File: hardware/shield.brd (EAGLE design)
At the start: 100 x 80 mm, 21 parts

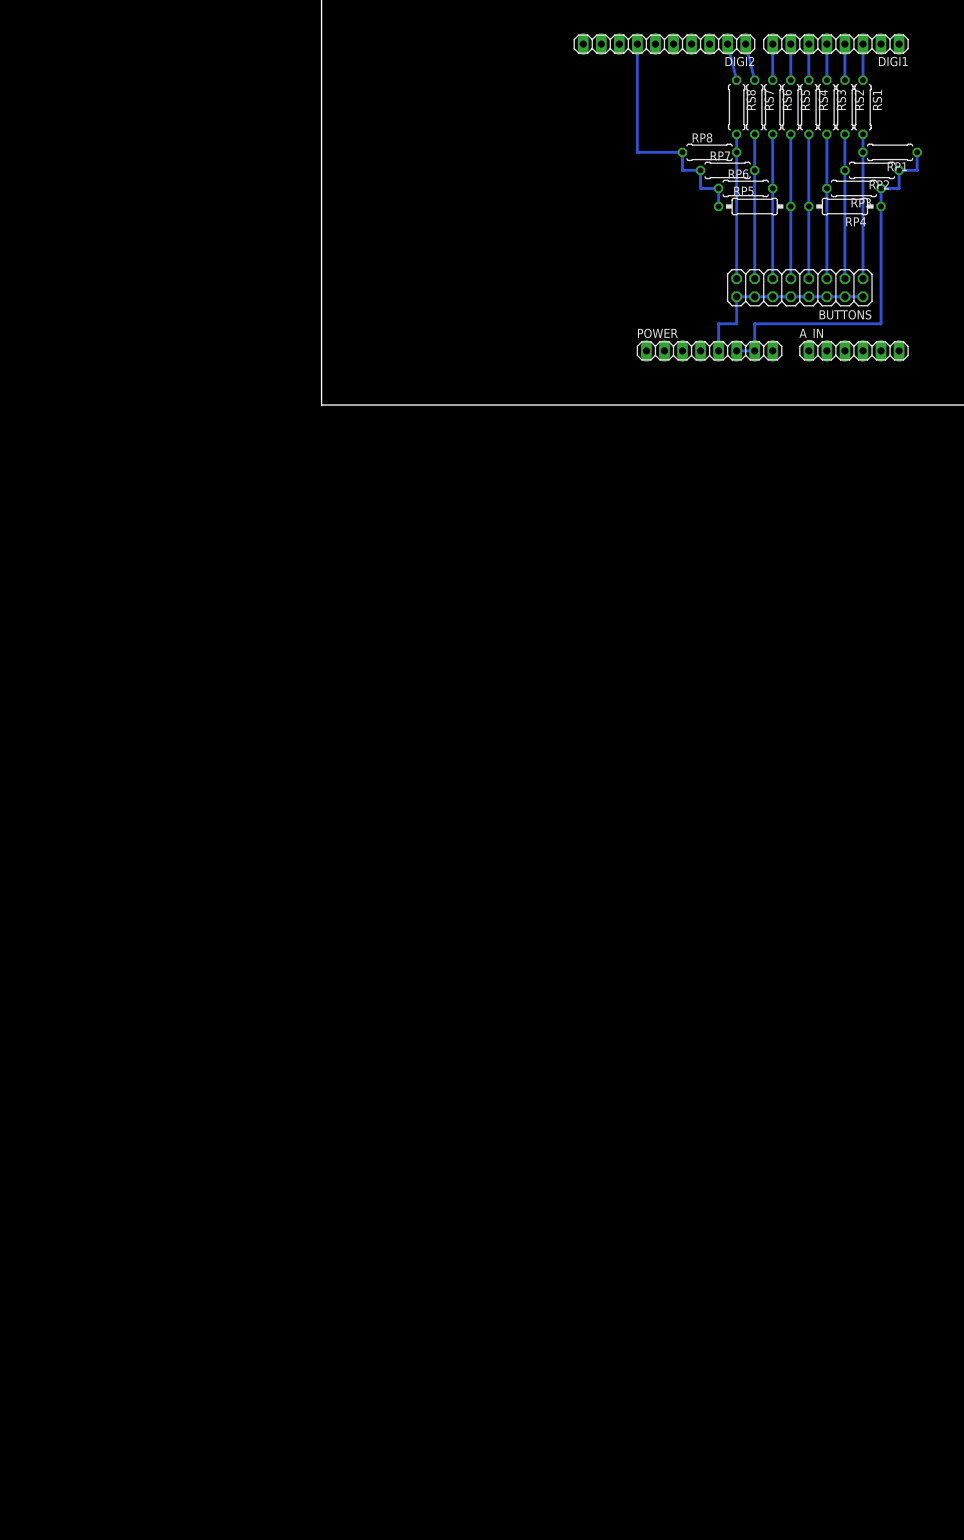
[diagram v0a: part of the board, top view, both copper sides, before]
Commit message: add poti connetions to schematic
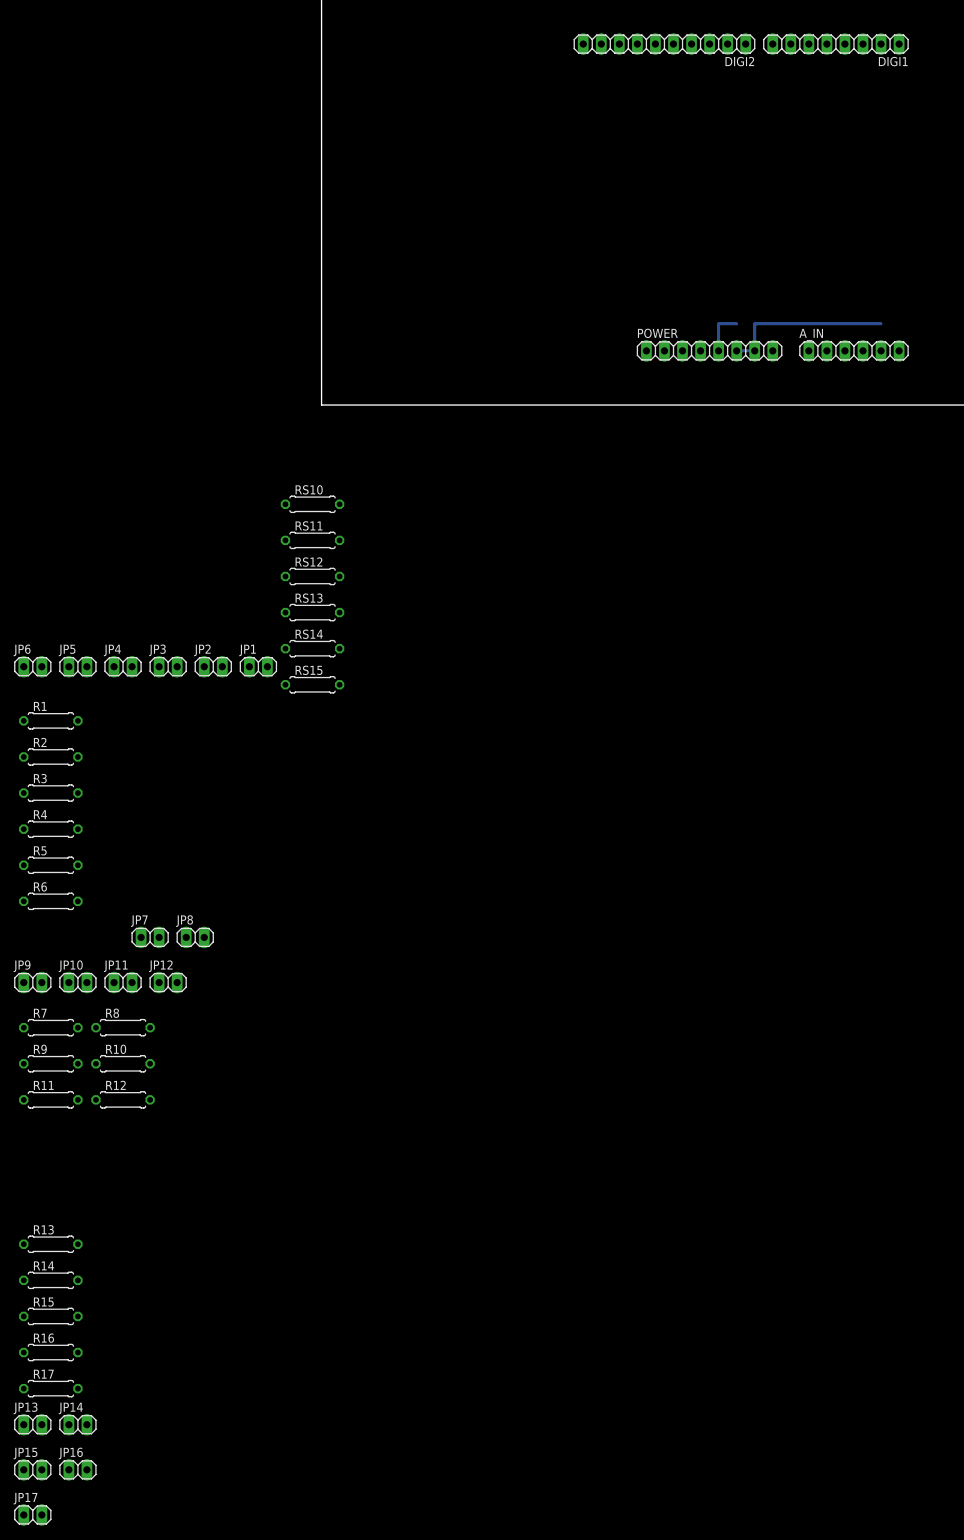
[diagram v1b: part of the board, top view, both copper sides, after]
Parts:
- removed BUTTONS: (no value), pinhead:2X08
- removed RP1, RP2, RP3, RP6, RP7, RP8: 10k, rcl:0207/7
- removed RP4, RP5: 10k, rcl:0207/10
- removed RS1, RS2, RS3, RS4, RS5, RS6, RS7, RS8: 100, rcl:0207/7
- added JP1, JP10, JP11, JP12, JP13, JP14, JP15, JP16, JP17, JP2, JP3, JP4, JP5, JP6, JP7, JP8, JP9: (no value), pinhead:1X02
- added R1, R2, R3, R4, R5, R6: (no value), rcl:0207/7
- added R10, R11, R12, R13, R14, R15, R16, R17, R7, R8, R9: 100, rcl:0207/7
- added RS10, RS11, RS12, RS13, RS14, RS15: 100k, rcl:0207/7
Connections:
- net RX1 renamed RX
- net TX1 renamed TX
- removed net B1: BUTTONS.1, RP1.2, RS1.2
- removed net B2: BUTTONS.3, RP2.2, RS2.2
- removed net B3: BUTTONS.5, RP3.2, RS3.2
- removed net B4: BUTTONS.7, RP4.2, RS4.2
- removed net B5: BUTTONS.9, RP5.2, RS5.2
- removed net B6: BUTTONS.11, RP6.2, RS6.2
- removed net B7: BUTTONS.13, RP7.2, RS7.2
- removed net B8: BUTTONS.15, RP8.2, RS8.2
- new net A10: JP17.1, R13.2
- new net A6: JP13.1, R17.2
- new net A7: JP14.1, R16.2
- new net A8: JP15.1, R15.2
- new net A9: JP16.1, R14.2
- new net N$1: JP13.2
- new net VCC: RS10.2, RS11.2, RS12.2, RS13.2, RS14.2, RS15.2
- net 5V: no longer BUTTONS.10, BUTTONS.12, BUTTONS.14, BUTTONS.16, BUTTONS.2, BUTTONS.4, BUTTONS.6, BUTTONS.8
- net A0: now also A_IN.1, JP1.1, JP7.1, R1.2, R6.1, R7.2, RS15.1; no longer A_IN.6
- net A1: now also A_IN.2, JP2.1, JP8.1, R2.2, R5.1, R8.2, RS14.1; no longer A_IN.5
- net A2: now also A_IN.3, JP3.1, JP9.1, R3.2, R4.1, R9.2, RS10.1; no longer A_IN.4
- net A3: now also A_IN.4, JP10.1, JP4.1, R10.2, R3.1, R4.2, RS11.1; no longer A_IN.3
- net A4: now also A_IN.5, JP11.1, JP5.1, R11.2, R2.1, R5.2, RS12.1; no longer A_IN.2
- net A5: now also A_IN.6, JP12.1, JP6.1, R1.1, R12.2, R6.2, RS13.1; no longer A_IN.1
- net D10: now also R15.1
- net D11: now also R16.1
- net D12: now also R17.1
- net D2: now also R12.1; no longer RS1.1
- net D3: now also R11.1; no longer RS2.1
- net D4: now also R10.1; no longer RS3.1
- net D5: now also R9.1; no longer RS4.1
- net D6: now also R8.1; no longer RS5.1
- net D7: now also R7.1; no longer RS6.1
- net D8: now also R13.1; no longer RS7.1
- net D9: now also R14.1; no longer RS8.1
- net GND: now also JP1.2, JP10.2, JP11.2, JP12.2, JP14.2, JP15.2, JP16.2, JP17.2, JP2.2, JP3.2, JP4.2, JP5.2, JP6.2, JP7.2, JP8.2, JP9.2; no longer RP1.1, RP2.1, RP3.1, RP4.1, RP5.1, RP6.1, RP7.1, RP8.1
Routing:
- net GND: track 87.6 -> 24.1 mm
- net 5V: track 27.9 -> 6.35 mm
- net B8: track 20.3 -> 0.00 mm
- net B7: track 20.3 -> 0.00 mm
- net B6: track 20.3 -> 0.00 mm
- net B5: track 20.3 -> 0.00 mm
- net B4: track 20.3 -> 0.00 mm
- net B3: track 20.3 -> 0.00 mm
- net B2: track 20.3 -> 0.00 mm
- net B1: track 20.3 -> 0.00 mm
- net D9: track 5.24 -> 0.00 mm
- net D8: track 5.24 -> 0.00 mm
- net D7: track 5.08 -> 0.00 mm
- net D6: track 5.08 -> 0.00 mm
- net D5: track 5.08 -> 0.00 mm
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
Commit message: add poti driving circuit to schematic and layout.
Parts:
- removed JP10, JP11, JP12, JP13, JP14, JP15, JP16, JP17, JP2, JP3, JP4, JP5, JP6, JP7, JP8, JP9: (no value), pinhead:1X02
- removed RS10, RS11, RS12, RS13, RS14, RS15: 100k, rcl:0207/7
- added MODULE1, MODULE2, MODULE3, MODULE4, MODULE5, MODULE6, MODULE7, MODULE8: (no value), pinhead:1X03
- added PRESET: (no value), pinhead:1X04
- added R18, R19, R20, R21, R22, R23: 100k, rcl:0207/7
- added R24: 10k, rcl:0207/7
- R1, R2, R3, R4, R5, R6: value (none) -> 100
- moved R17 226.7 mm to (57.1, 67.3), turned to 270 degrees
- moved R16 223.2 mm to (59.7, 67.3), turned to 270 degrees
- moved R15 219.8 mm to (62.2, 67.3), turned to 270 degrees
- moved R14 216.5 mm to (64.8, 67.3), turned to 270 degrees
- moved R13 213.3 mm to (67.3, 67.3), turned to 270 degrees
- moved R11 203.7 mm to (81.3, 67.3), turned to 270 degrees
- moved R12 199.4 mm to (83.8, 67.3), turned to 270 degrees
- moved R9 196.6 mm to (76.2, 67.3), turned to 270 degrees
- moved R10 192.3 mm to (78.7, 67.3), turned to 270 degrees
- moved R7 189.6 mm to (71.1, 67.3), turned to 270 degrees
- moved R8 185.3 mm to (73.7, 67.3), turned to 270 degrees
- moved R6 137.3 mm to (68.6, 16.5), turned to 90 degrees
- moved R5 136.1 mm to (71.1, 16.5), turned to 90 degrees
- moved R4 135.3 mm to (73.7, 16.5), turned to 90 degrees
- moved R3 134.6 mm to (76.2, 16.5), turned to 90 degrees
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- renumbered A_IN to ANALOG
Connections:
- removed net 5V: POWER.5
- removed net A10: JP17.1, R13.2
- removed net A6: JP13.1, R17.2
- removed net A7: JP14.1, R16.2
- removed net A8: JP15.1, R15.2
- removed net A9: JP16.1, R14.2
- removed net N$1: JP13.2
- new net LED: JP1.2, R24.2
- new net N.C.: MODULE8.3, PRESET.4
- new net XA0: MODULE5.3, R23.1, R6.2
- new net XA1: MODULE6.3, R22.1, R5.2
- new net XA2: MODULE1.3, R21.1, R4.2
- new net XA3: MODULE2.3, R20.1, R3.2
- new net XA4: MODULE3.3, R19.1, R2.2
- new net XA5: MODULE4.3, R1.2, R18.1
- new net XD0: PRESET.2, R17.2
- new net XD1: PRESET.3, R16.2
- new net XD10: MODULE8.2, R15.2
- new net XD2: MODULE1.2, R12.2
- new net XD3: MODULE2.2, R11.2
- new net XD4: MODULE3.2, R10.2
- new net XD5: MODULE4.2, R9.2
- new net XD6: MODULE5.2, R8.2
- new net XD7: MODULE6.2, R7.2
- new net XD8: MODULE7.2, R13.2
- new net XD9: MODULE7.3, R14.2
- net 3.3V: now also POWER.5; no longer POWER.4
- net A0: no longer JP1.1, JP7.1, R1.2, R7.2, RS15.1
- net A1: no longer JP2.1, JP8.1, R2.2, R8.2, RS14.1
- net A2: no longer JP3.1, JP9.1, R3.2, R9.2, RS10.1
- net A3: no longer JP10.1, JP4.1, R10.2, R4.2, RS11.1
- net A4: no longer JP11.1, JP5.1, R11.2, R5.2, RS12.1
- net A5: no longer JP12.1, JP6.1, R12.2, R6.2, RS13.1
- net D13: now also R24.1
- net GND: now also JP1.1, MODULE1.1, MODULE2.1, MODULE3.1, MODULE4.1, MODULE5.1, MODULE6.1, MODULE7.1, MODULE8.1, POWER.2, POWER.3, PRESET.1; no longer JP1.2, JP10.2, JP11.2, JP12.2, JP14.2, JP15.2, JP16.2, JP17.2, JP2.2, JP3.2, JP4.2, JP5.2, JP6.2, JP7.2, JP8.2, JP9.2, POWER.6, POWER.7
- net IOREF: now also POWER.7; no longer POWER.2
- net RESET: now also POWER.6; no longer POWER.3
- net VCC: now also POWER.4, R18.2, R19.2, R20.2, R21.2, R22.2, R23.2; no longer RS10.2, RS11.2, RS12.2, RS13.2, RS14.2, RS15.2
- net VIN: now also POWER.1; no longer POWER.8
- net _: now also POWER.8; no longer POWER.1
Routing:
- net GND: track 24.1 -> 0.00 mm
- net 5V: track 6.35 -> 0.00 mm

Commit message: small changes in schematic and layout
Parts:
- removed JP1: (no value), pinhead:1X02
- added LIGHT: (no value), pinhead:1X02
- PRESET: device pinhead:1X04 -> pinhead:1X03
- moved R24 92.0 mm to (54.6, 67.3), turned to 270 degrees
- moved PRESET 22.7 mm to (57.1, 54.6), turned to 0 degrees
- moved MODULE6 17.8 mm to (83.8, 47.0)
- moved POWER 8.89 mm to (57.1, 7.62)
- moved MODULE7 3.81 mm to (66.0, 47.0)
- moved MODULE5 3.81 mm to (81.3, 47.0)
- moved MODULE8 3.81 mm to (62.2, 47.0)
- moved R20 3.59 mm to (74.9, 33.0)
- moved R18 3.59 mm to (80.0, 38.1)
- moved R21 3.59 mm to (72.4, 30.5)
- moved R23 3.59 mm to (67.3, 25.4)
- moved R22 3.59 mm to (69.8, 27.9)
- moved R19 3.59 mm to (77.5, 35.6)
- moved MODULE4 2.54 mm to (78.7, 47.0)
- moved R2 2.54 mm to (81.3, 16.5)
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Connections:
- net GND: now also LIGHT.1; no longer JP1.1
- net LED: now also LIGHT.2; no longer JP1.2
- net N.C.: no longer PRESET.4
- net XA0: now also MODULE1.3; no longer MODULE5.3
- net XA1: now also MODULE2.3; no longer MODULE6.3
- net XA2: no longer MODULE1.3
- net XA3: now also MODULE3.3, MODULE4.3; no longer MODULE2.3
- net XA4: now also MODULE5.3; no longer MODULE3.3
- net XA5: now also MODULE6.3; no longer MODULE4.3
- net XD2: now also MODULE6.2; no longer MODULE1.2
- net XD3: now also MODULE5.2; no longer MODULE2.2
- net XD4: now also MODULE4.2; no longer MODULE3.2
- net XD5: now also MODULE3.2; no longer MODULE4.2
- net XD6: now also MODULE2.2; no longer MODULE5.2
- net XD7: now also MODULE1.2; no longer MODULE6.2

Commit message: get potis to work...
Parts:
- R18, R19, R20, R21, R22, R23: value 100k -> 1k
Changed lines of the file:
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@@
 <element name="DIGI1" library="pinhead" package="1X08" value="" x="80.01" y="77.47" rot="R180"/>
 <element name="DIGI2" library="pinhead" package="1X10" value="" x="55.88" y="77.47" rot="R180"/>
-<element name="R20" library="rcl" package="0207/7" value="100k" x="74.93" y="33.02" rot="R180"/>
-<element name="R21" library="rcl" package="0207/7" value="100k" x="72.39" y="30.48" rot="R180"/>
-<element name="R22" library="rcl" package="0207/7" value="100k" x="69.85" y="27.94" rot="R180"/>
-<element name="R23" library="rcl" package="0207/7" value="100k" x="67.31" y="25.4" rot="R180"/>
-<element name="R19" library="rcl" package="0207/7" value="100k" x="77.47" y="35.56" rot="R180"/>
-<element name="R18" library="rcl" package="0207/7" value="100k" x="80.01" y="38.1" rot="R180"/>
+<element name="R20" library="rcl" package="0207/7" value="1k" x="74.93" y="33.02" rot="R180"/>
+<element name="R21" library="rcl" package="0207/7" value="1k" x="72.39" y="30.48" rot="R180"/>
+<element name="R22" library="rcl" package="0207/7" value="1k" x="69.85" y="27.94" rot="R180"/>
+<element name="R23" library="rcl" package="0207/7" value="1k" x="67.31" y="25.4" rot="R180"/>
+<element name="R19" library="rcl" package="0207/7" value="1k" x="77.47" y="35.56" rot="R180"/>
+<element name="R18" library="rcl" package="0207/7" value="1k" x="80.01" y="38.1" rot="R180"/>
 <element name="R1" library="rcl" package="0207/7" value="100" x="83.82" y="16.51" rot="R90"/>
 <element name="R2" library="rcl" package="0207/7" value="100" x="81.28" y="16.51" rot="R90"/>
